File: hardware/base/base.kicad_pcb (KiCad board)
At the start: 4 copper layers, 60 x 60 mm, 66 parts, among them J1 Debug, J2 USB_B_Mini, J3 Serial Interface, J4 SWD, J5 OLED Display, M1 Fan_ALT, Q1 Q_NMOS_GSD, Q2 Q_NMOS_GSD, Q3 Q_NMOS_GSD, SW3 RotaryEncoder_Switch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

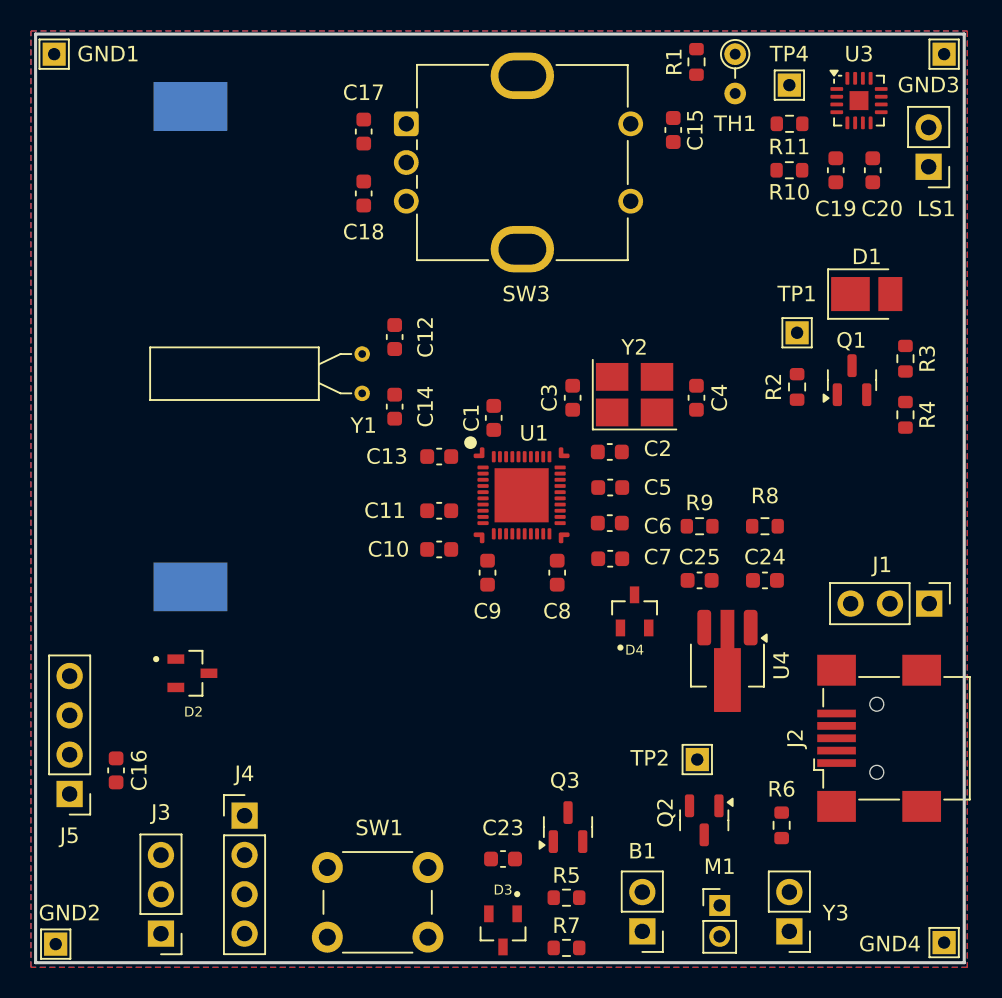
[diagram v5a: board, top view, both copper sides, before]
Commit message: Finish front layer traces
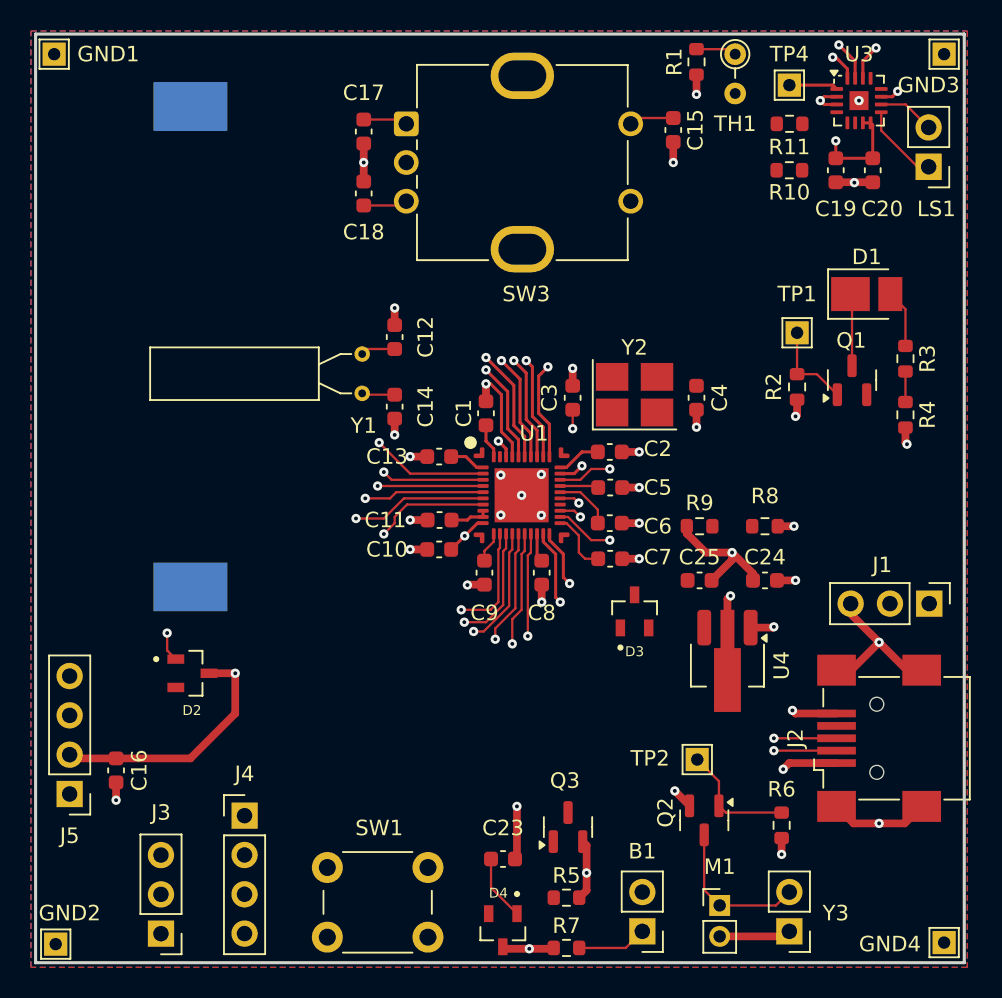
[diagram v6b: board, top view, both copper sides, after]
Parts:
- D2, D3, D4: value D_Schottky -> D_Schottky_1_3
- moved D3 22.3 mm to (159.0, 57.0), turned to 90 degrees
- moved D4 22.3 mm to (150.5, 77.6), turned to -90 degrees
- moved C8 1.00 mm to (153.0, 54.5)
- moved C11 0.60 mm to (146.4, 51.1)
- moved C1 0.58 mm to (149.4, 44.2)
- moved C9 0.20 mm to (149.3, 54.5)
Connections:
- B1 pad 2: Net-(D3-A) -> Net-(D4-A)
- C23 pad 2: Net-(D3-A) -> Net-(D4-A)
- C25 pad 1: Net-(D4-A) -> Net-(D3-A)
- D2 pad 1: +3.3V -> Net-(BT1-+)
- D2 pad 2: Net-(BT1-+) -> (no net)
- D2 pad 3: (no net) -> +3.3V
- D3 pad 1: /VBUS -> Net-(D3-A)
- D3 pad 2: Net-(D3-A) -> (no net)
- D3 pad 3: (no net) -> +3.3V
- D4 pad 1: +3.3V -> Net-(D4-A)
- D4 pad 2: Net-(D4-A) -> (no net)
- D4 pad 3: (no net) -> /VBUS
- Q3 pad 3: Net-(D3-A) -> Net-(D4-A)
- U4 pad 3: Net-(D4-A) -> Net-(D3-A)
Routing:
- net GND: track 0.00 -> 73.0 mm, vias 0 -> 37
- net /VBUS: track 0.00 -> 29.6 mm, vias 0 -> 9
- net +3.3V: track 0.00 -> 27.5 mm, vias 0 -> 2
- net Net-(J2-D+): track 0.00 -> 11.7 mm, vias 0 -> 2
- net Net-(J2-D-): track 0.00 -> 11.1 mm, vias 0 -> 2
- net /ROT_ENC_A: track 0.00 -> 10.3 mm, vias 0 -> 1
- net /AMP_LRCLK: track 0.00 -> 10.1 mm, vias 0 -> 2
- net /ROT_ENC_B: track 0.00 -> 9.86 mm, vias 0 -> 1
- net Net-(M1-+): track 0.00 -> 9.84 mm
- net /ROT_ENC_S1: track 0.00 -> 9.74 mm, vias 0 -> 1
- net Net-(U1-P0.00/XL1): track 0.00 -> 9.67 mm, vias 0 -> 1
- net /LED: track 0.00 -> 9.66 mm, vias 0 -> 1
- net /AMP_DIN: track 0.00 -> 9.65 mm, vias 0 -> 1
- net /AMP_FAN_HUM: track 0.00 -> 9.28 mm, vias 0 -> 1
- net Net-(U1-AIN1/P0.03): track 0.00 -> 8.98 mm, vias 0 -> 1
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
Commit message: Finish traces
Few warnings left
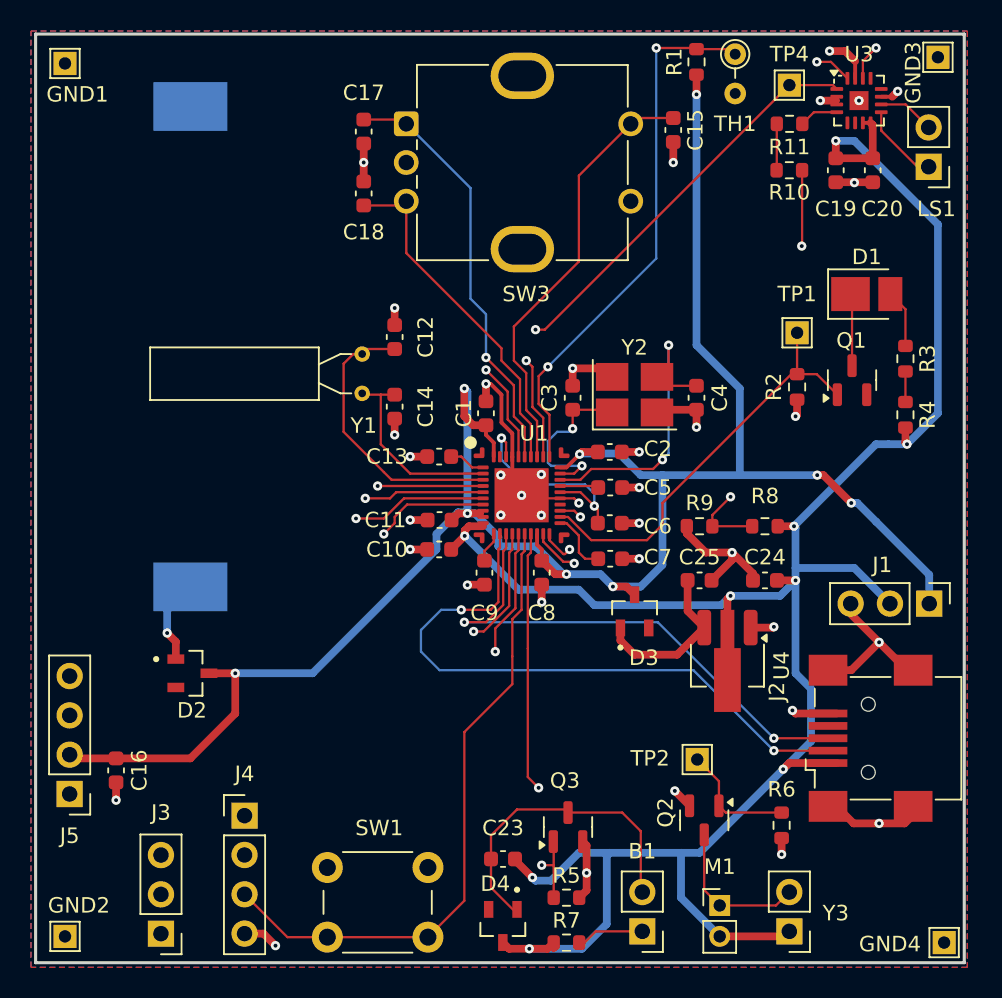
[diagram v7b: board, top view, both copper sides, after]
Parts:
- moved GND1 0.92 mm to (122.2, 21.6)
- moved GND2 0.78 mm to (122.2, 78.0)
- moved J2 0.55 mm to (174.1, 65.2)
- moved GND3 0.45 mm to (178.6, 21.2)
- moved R7 0.35 mm to (154.6, 78.4)
- moved D4 0.28 mm to (150.5, 77.3)
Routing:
- net /VBUS: track 29.6 -> 146.0 mm
- net +3.3V: track 27.5 -> 136.5 mm, vias 2 -> 9
- net /AMP_BCLK: track 8.68 -> 63.7 mm
- net /AMP_LRCLK: track 10.1 -> 63.7 mm
- net /AMP_FAN_HUM: track 9.28 -> 62.0 mm, vias 1 -> 2
- net Net-(J3-Pin_1): track 7.73 -> 44.8 mm
- net Net-(J4-Pin_3): track 7.44 -> 41.6 mm, vias 1 -> 0
- net Net-(J3-Pin_2): track 7.43 -> 40.4 mm
- net Net-(J4-Pin_2): track 4.87 -> 36.3 mm
- net Net-(J2-D-): track 11.1 -> 41.1 mm
- net Net-(J4-Pin_1): track 3.75 -> 33.5 mm
- net /AMP_DIN: track 9.65 -> 36.9 mm, vias 1 -> 2
- net Net-(U1-AIN1/P0.03): track 8.98 -> 35.1 mm, vias 1 -> 2
- net Net-(J5-Pin_3): track 7.43 -> 32.6 mm
- net Net-(J5-Pin_4): track 8.75 -> 33.5 mm
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
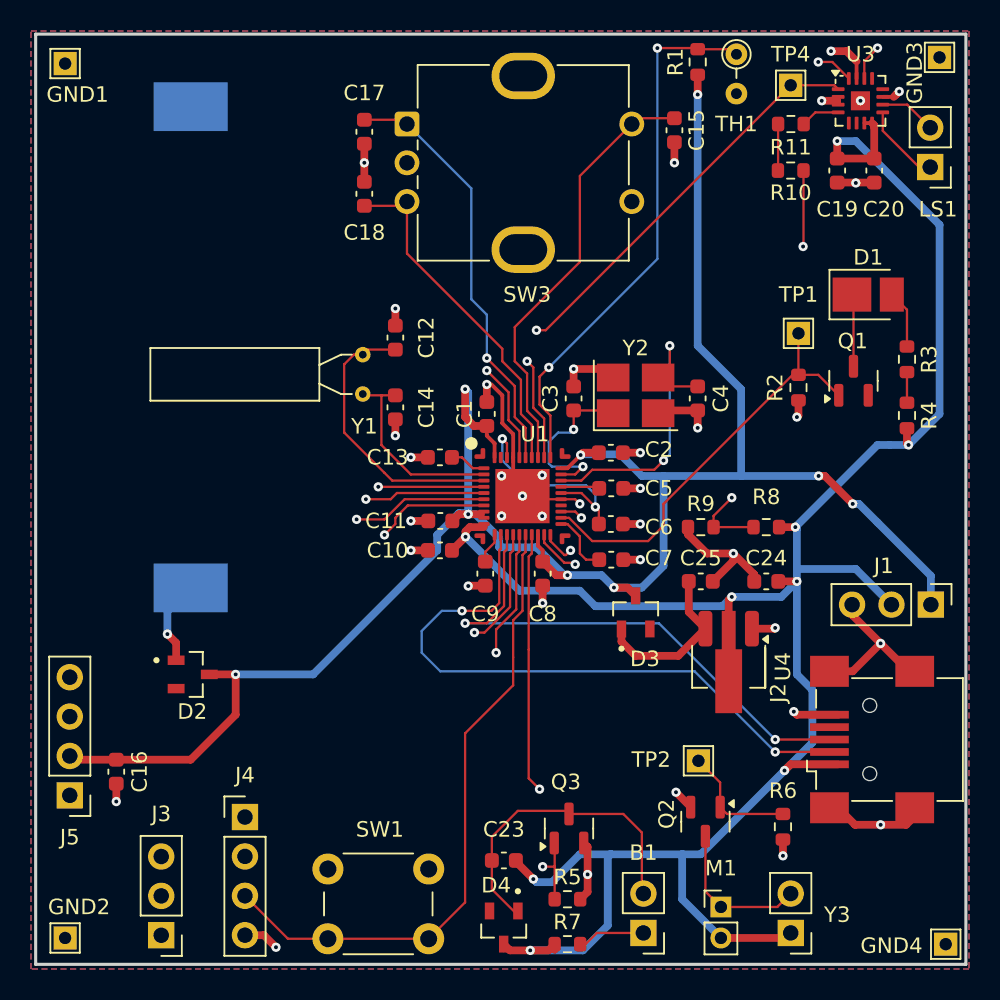
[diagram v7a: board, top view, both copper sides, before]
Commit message: add mounting holes
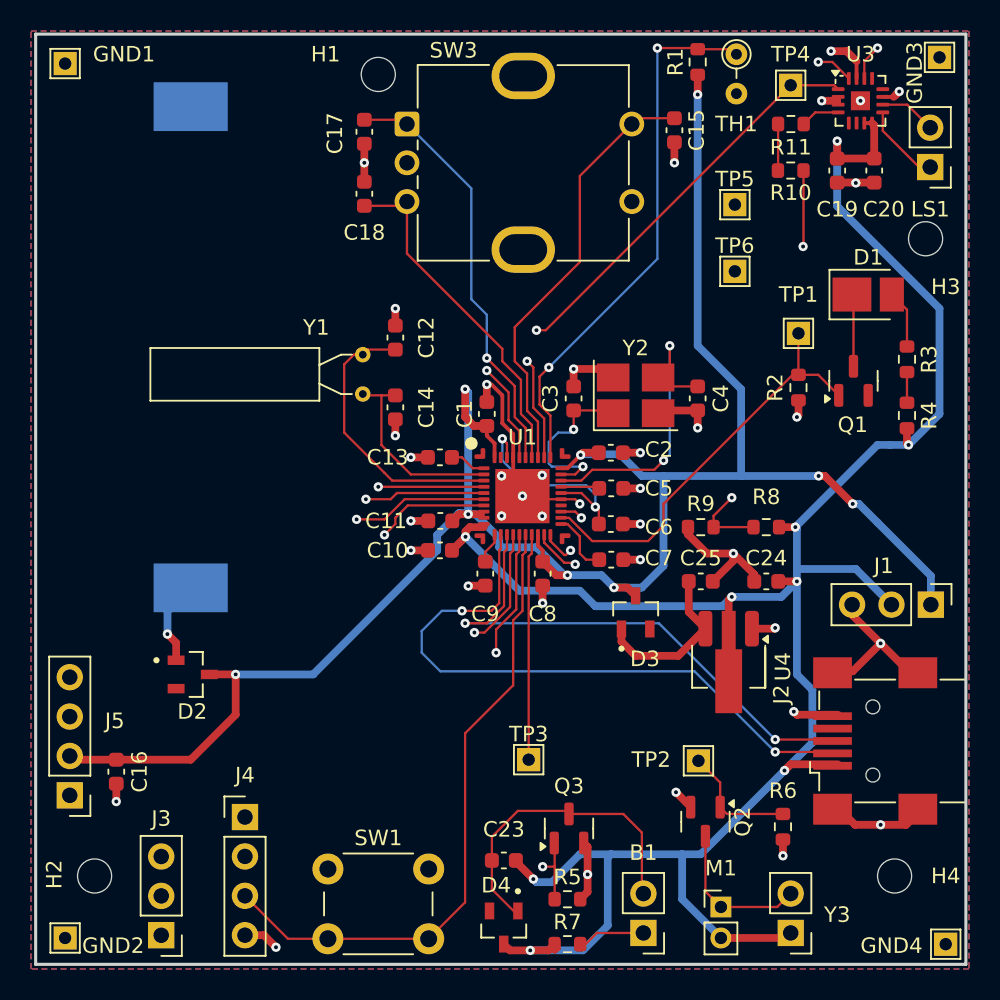
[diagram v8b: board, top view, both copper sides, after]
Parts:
- added H1: MountingHole, MountingHole:MountingHole_2.2mm_M2_ISO7380, F.Cu at (142.4, 22.3)
- added H2: MountingHole, MountingHole:MountingHole_2.2mm_M2_ISO7380, F.Cu at (124.1, 74.0)
- added H3: MountingHole, MountingHole:MountingHole_2.2mm_M2_ISO7380, F.Cu at (177.7, 32.9)
- added H4: MountingHole, MountingHole:MountingHole_2.2mm_M2_ISO7380, F.Cu at (175.7, 74.0)
- added TP3: TestPoint, E7020E:TestPoint_THTPad_1.5x1.5mm_Drill0.8mm, F.Cu at (152.1, 66.5)
- added TP5: TestPoint, E7020E:TestPoint_THTPad_1.5x1.5mm_Drill0.8mm, F.Cu at (165.4, 30.7)
- added TP6: TestPoint, E7020E:TestPoint_THTPad_1.5x1.5mm_Drill0.8mm, F.Cu at (165.4, 35.0)
- moved J2 0.22 mm to (174.3, 65.3)
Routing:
- net /AMP_BCLK: track 63.7 -> 56.0 mm
- net Net-(J3-Pin_1): track 44.8 -> 43.5 mm
- net /VBUS: track 146.0 -> 145.3 mm
- net /HAPTIC: vias 2 -> 1
